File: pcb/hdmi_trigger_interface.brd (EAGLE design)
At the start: 78.7 x 63.5 mm, 58 parts, among them U1 TPD12S016PWR, U2 TPD12S016PWR, Y1 SI514

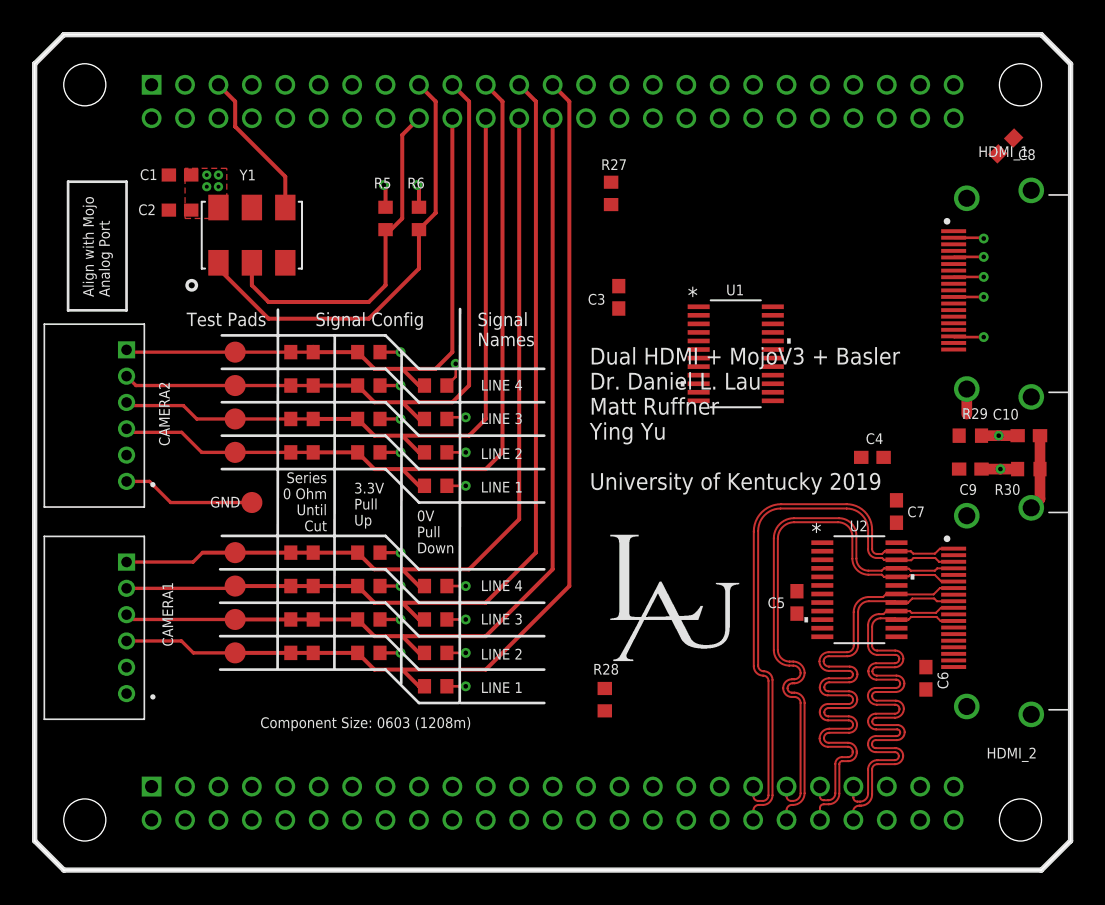
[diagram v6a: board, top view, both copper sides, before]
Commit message: hdmi differential pairs routed and length tunedgit status
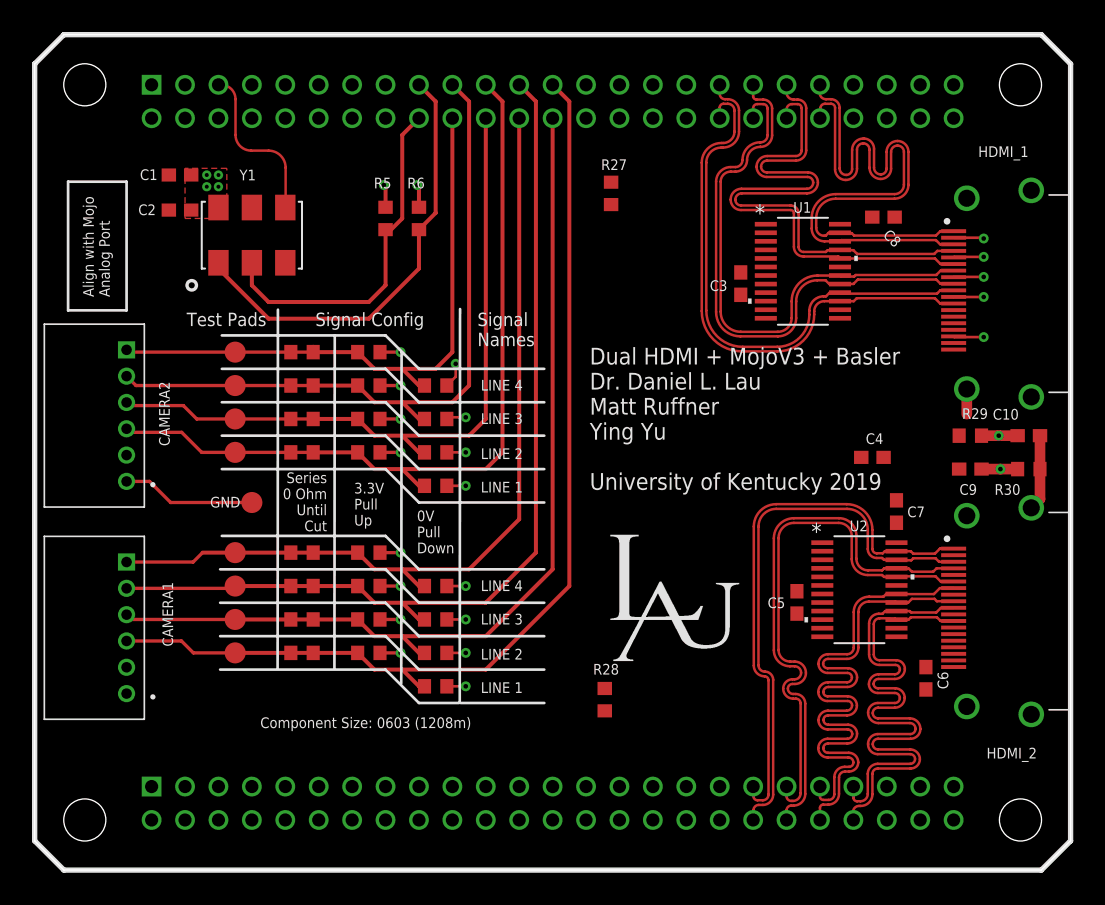
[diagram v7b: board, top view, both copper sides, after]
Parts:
- moved C8 10.8 mm to (64.5, 49.6), turned to 0 degrees
- moved C3 9.33 mm to (53.7, 44.6)
- moved U1 8.09 mm to (58.4, 45.5)
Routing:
- net D11_P: track 0.00 -> 41.4 mm
- net D11_N: track 0.00 -> 41.4 mm
- net D01_N: track 0.00 -> 41.2 mm
- net D21_N: track 0.00 -> 41.1 mm
- net D01_P: track 0.00 -> 41.1 mm
- net D21_P: track 0.00 -> 41.1 mm
- net CLK1_P: track 0.01 -> 41.0 mm
- net CLK1_N: track 0.00 -> 41.0 mm
- net PROG_CLK: track 11.4 -> 12.3 mm
